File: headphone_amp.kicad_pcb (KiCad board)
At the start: 4 copper layers, 60 x 60 mm, 133 parts, among them J1 USB4085-GF-A, J10 AudioJack2, J2 JST PH2, J3 JST GH2, J4 JST SH3, J5 Header_2x1, J6 JST SH3, J7 415-47-208-41-004000, J8 SJ-3523-SMT-TR, Q1 BSS138, SW1 SW_SPST, U1 BQ24074RGTR, U2 OPA1678, U3 OPA1622, U4 TLE2426xD, U5 TPS61379QWRTERQ1, U6 CD74HC4060, U7 74HC14BQ,115, U8 74HC02, U9 TLV7A0325PDBVR

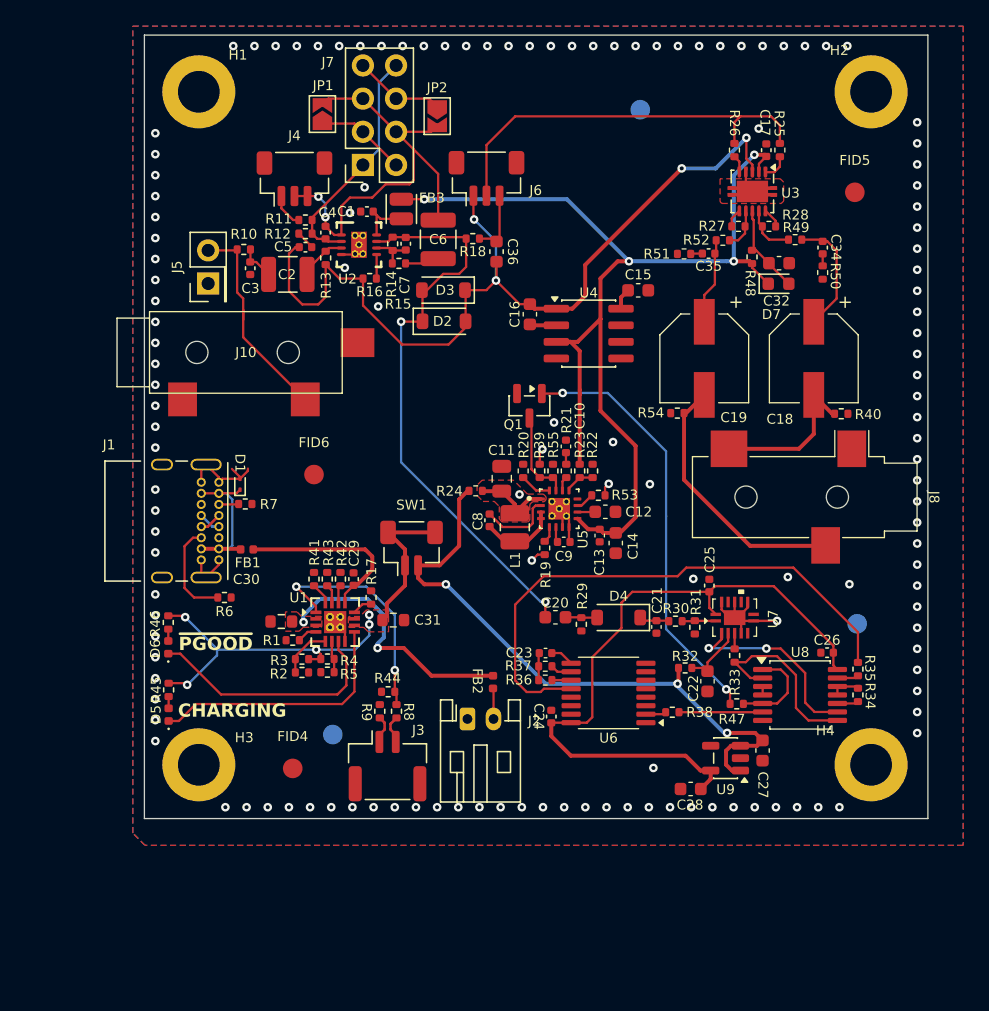
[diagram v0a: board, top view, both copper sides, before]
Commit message: Picked off the board parts and ordered on DigiKey -- also added notes on schematic.
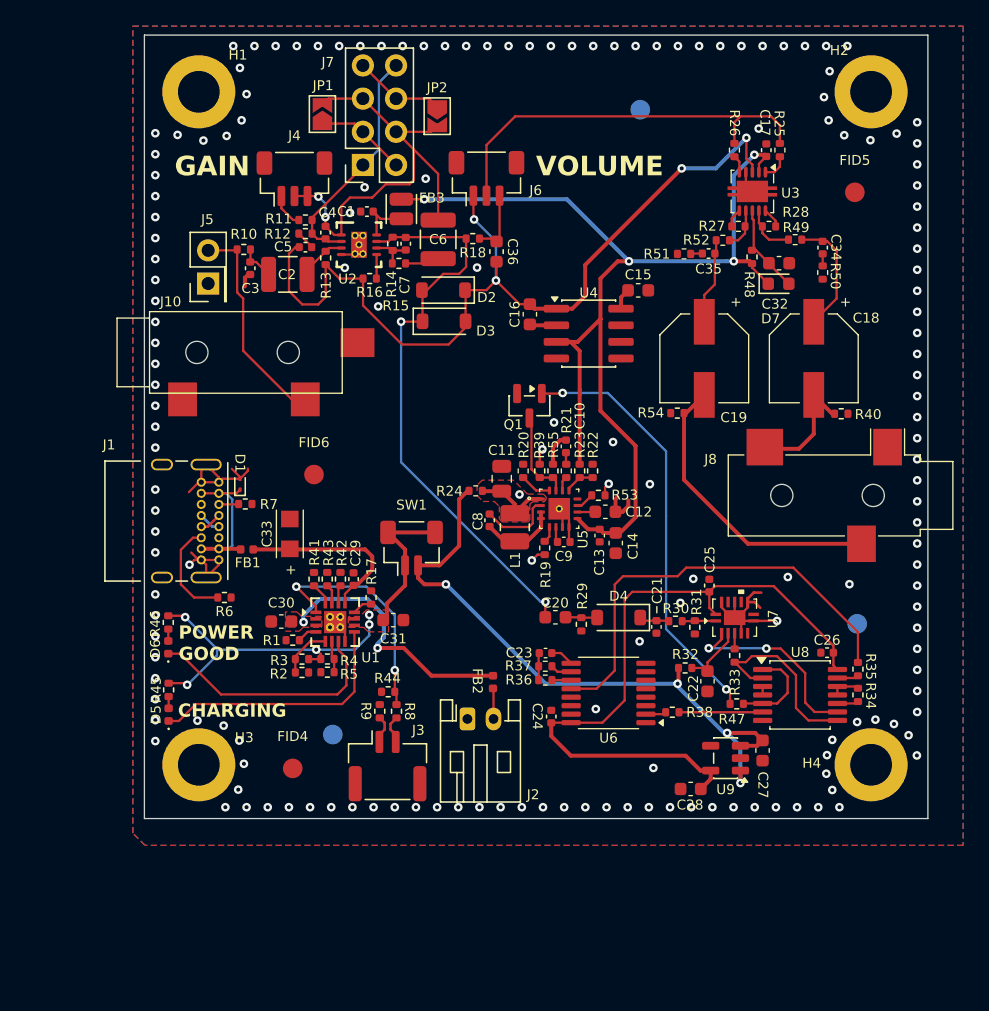
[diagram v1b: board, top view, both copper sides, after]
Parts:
- added C33: TCJA106M016R0200, polymers:TCJA_AVX, F.Cu at (57.1, 67.5)
- C18, C19: footprint cap_polymer:WCAP-PSLP_6.3X5.8_DXL_ -> polymers:WCAP-PSLP_6.3X5.8_DXL_
- C30, C31: footprint Resistor_SMD:R_0603_1608Metric -> Capacitor_SMD:C_0603_1608Metric
- U3: footprint Package_SON:Texas_S-PVSON-N10 -> integrated_circuits:Texas_S-PVSON-N10
- moved J8 2.75 mm to (99.3, 64.6)
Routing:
- net GND: track 31.8 -> 46.9 mm, vias 131 -> 162
- net /Watchdog/WAKE: track 42.4 -> 34.0 mm
- net /Current Buffer/HEADPHONES_LEFT: track 12.2 -> 9.48 mm
- net /Current Buffer/HEADPHONES_RIGHT: track 20.2 -> 22.9 mm
- net /V_{SYS}: track 47.7 -> 49.3 mm, vias 3 -> 4
- net /Watchdog/V_{LOGIC}: track 51.6 -> 52.3 mm
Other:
- board text added: "GAIN"
- board text added: "POWER GOOD"
- board text added: "VOLUME"
- board text removed: "~{PGOOD}"

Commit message: Finilizing DRC and ERC
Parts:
- moved J5 2.06 mm to (48.8, 48.4)
- moved FB2 0.66 mm to (72.2, 79.3), turned to 180 degrees
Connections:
- net /AUDIO_BUFFER_IN renamed /Audio Input/AUDIO_OUT
- net /SHUTDOWN renamed /Boost/SHUTDOWN
- net /TS+ renamed /Battery Charger/TS+
- net /WD_AUDIO_IN renamed /Audio Input/SECOND_STAGE_OUT
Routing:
- net /Audio Input/JACK_IN: track 16.5 -> 18.6 mm
- net /V_{BAT}: track 20.3 -> 19.8 mm
- net GND: vias 162 -> 178
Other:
- board text added: "1"
- board text added: "2"
- board text added: "POWER INPUT"
- board text removed: "POWER GOOD"

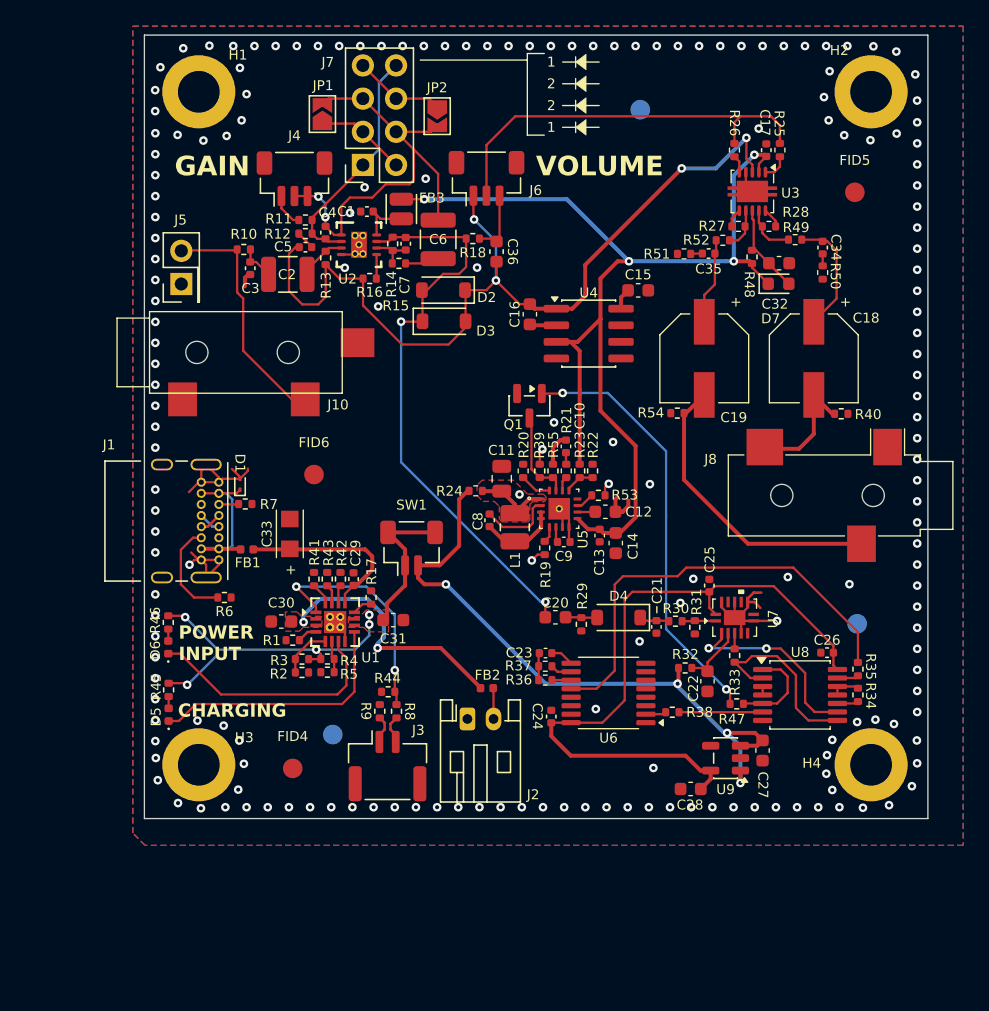
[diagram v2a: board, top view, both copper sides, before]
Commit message: Added dimensions, logo, and silkscreen information.
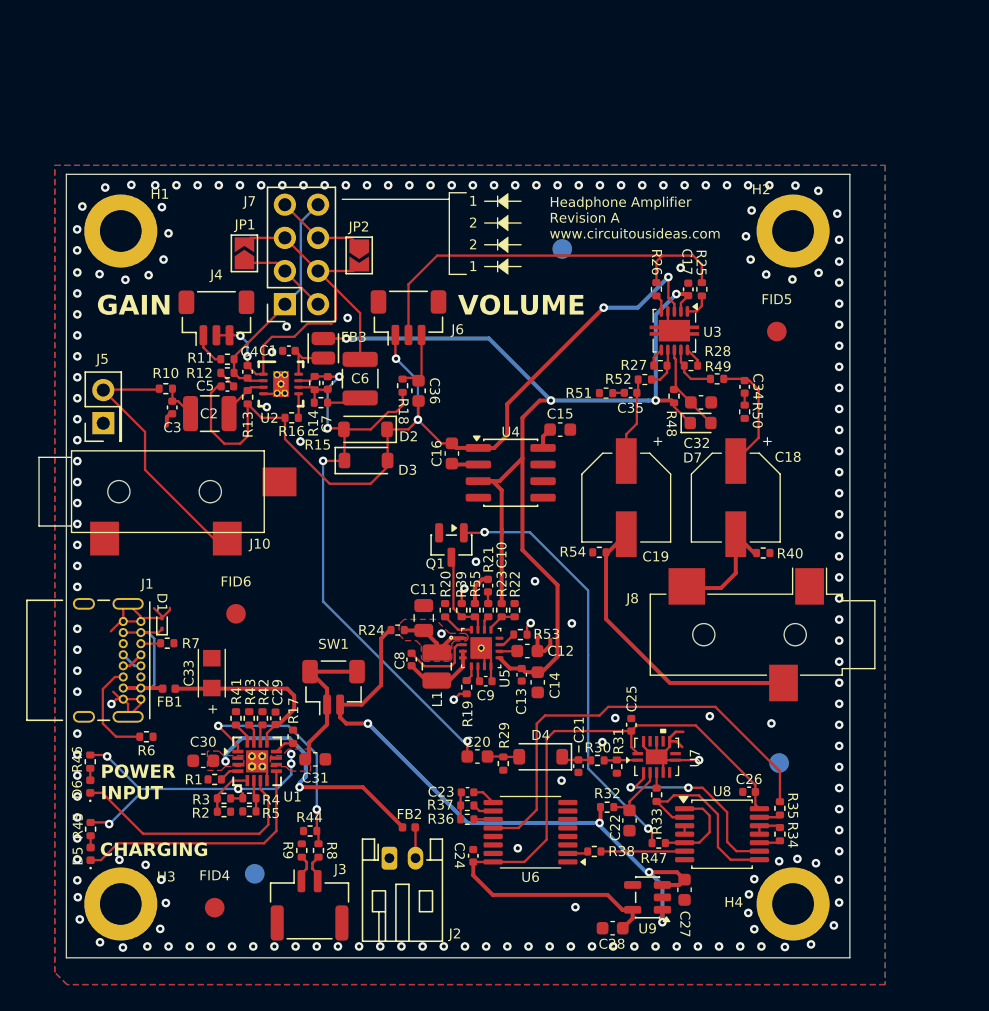
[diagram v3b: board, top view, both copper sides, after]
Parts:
- moved R18 12.5 mm to (65.8, 56.2), turned to 90 degrees
- moved C13 12.2 mm to (74.9, 78.3)
- moved C14 12.2 mm to (76.1, 78.9)
- moved C21 12.2 mm to (79.2, 85.3)
- moved C28 12.2 mm to (81.8, 97.7)
- moved D4 12.2 mm to (76.3, 84.6)
- moved FB2 12.2 mm to (66.2, 90.0)
- moved R34 12.2 mm to (94.6, 90.5)
- moved R45 12.2 mm to (41.9, 90.1)
- moved U7 12.2 mm to (85.2, 84.6)
- moved U8 12.2 mm to (90.2, 90.5)
- moved U9 12.2 mm to (84.5, 95.4)
- moved FID4 12.2 mm to (51.4, 96.2)
- moved R17 12.2 mm to (57.4, 83.1)
- moved R7 12.2 mm to (47.7, 75.9)
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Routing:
- net /Audio Input/SECOND_STAGE_OUT: track 44.8 -> 46.6 mm, vias 2 -> 4
- net /Audio Input/JACK_IN: track 18.6 -> 20.2 mm
- net GND: vias 178 -> 177
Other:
- board text added: "Headphone Amplifier Revision A www.circuitousideas.com"

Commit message: Worked with Claude to check BOM, prepare InvenTree import files.
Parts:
- C12: footprint Capacitor_SMD:C_0603_1608Metric -> Capacitor_SMD:C_0805_2012Metric
- moved C13 1.57 mm to (73.6, 79.2)
- moved C14 0.63 mm to (75.6, 78.5), turned to 180 degrees
- moved C12 0.35 mm to (75.5, 76.8)
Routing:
- net /V+: track 84.6 -> 90.3 mm
- net GND: track 46.9 -> 48.3 mm, vias 177 -> 178

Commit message: Finally updated all parts in InvenTree and linked them with KiCAD. Ready for BOM exports to JLC.
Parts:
- C33: value TCJA106M016R0200 -> 10uF
- D2, D3: value D -> 1N4148W
- D4: value 1N4148W-7-F -> 1N4148W
- FB3: value MDF2016BSS600CTD25 -> 60R @ 2MHz
- J10: value AudioJack2 -> MJ-3523-SMT-TR
- R20: value 18K -> 18.2K
- SW1: value SW_SPST -> JST SH2
- U4: value TLE2426xD -> TLE2426
- U7: value 74HC14BQ,115 -> 74HC14
- U9: value TLV7A0325PDBVR -> TLV7A0325
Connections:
- SW1 pad MP: /Battery Charger/OUT -> (no net)
- U7 pad 15: GND -> (no net)
- U7 pad 7: GND -> unconnected-(U7G-GND-Pad7)
